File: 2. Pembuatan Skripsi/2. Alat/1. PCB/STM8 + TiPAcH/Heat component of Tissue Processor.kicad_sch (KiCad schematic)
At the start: 57 parts, among them J1 Conn_01x02, J2 Sensors, J3 Screw_Terminal_01x02, J8 Conn_01x06, K1 EE2-4.5NU, Q1 S9013, Q2 S9013, Q3 S9013, Q4 MMBT2222, SW1 SW_SPST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

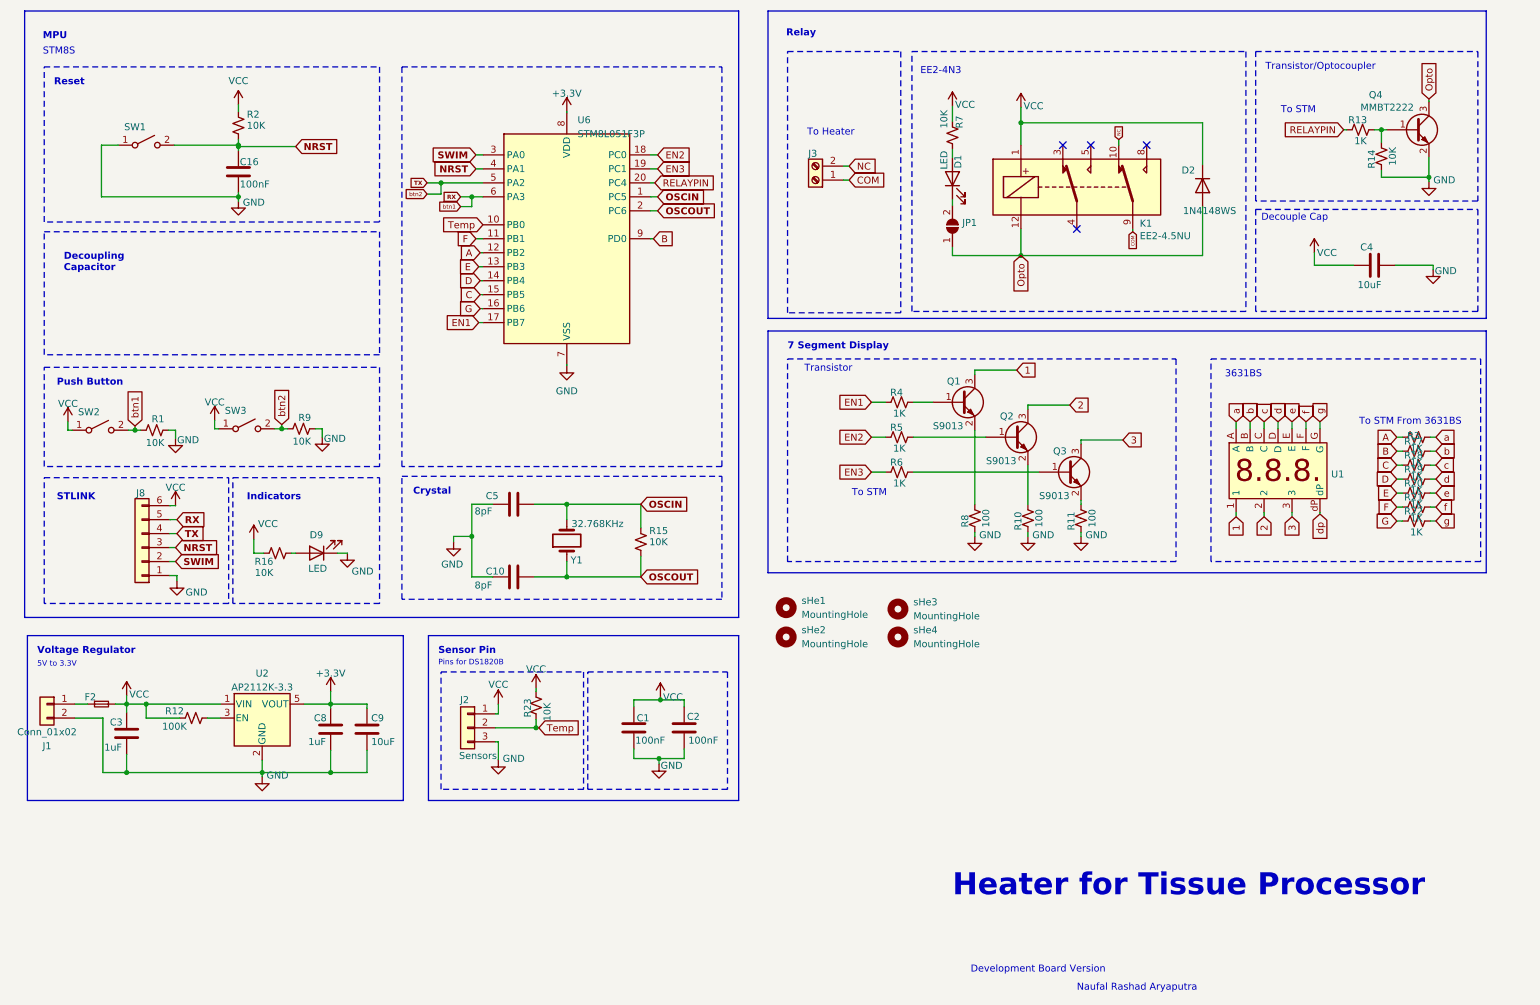
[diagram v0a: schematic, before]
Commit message: *Major Update*
- STM8S PCB jumpers are relocated to make it easier to solder it
- ATMEGA328 version is added and revised for backup option
- Arduino Code for ATMEGA328 is added.
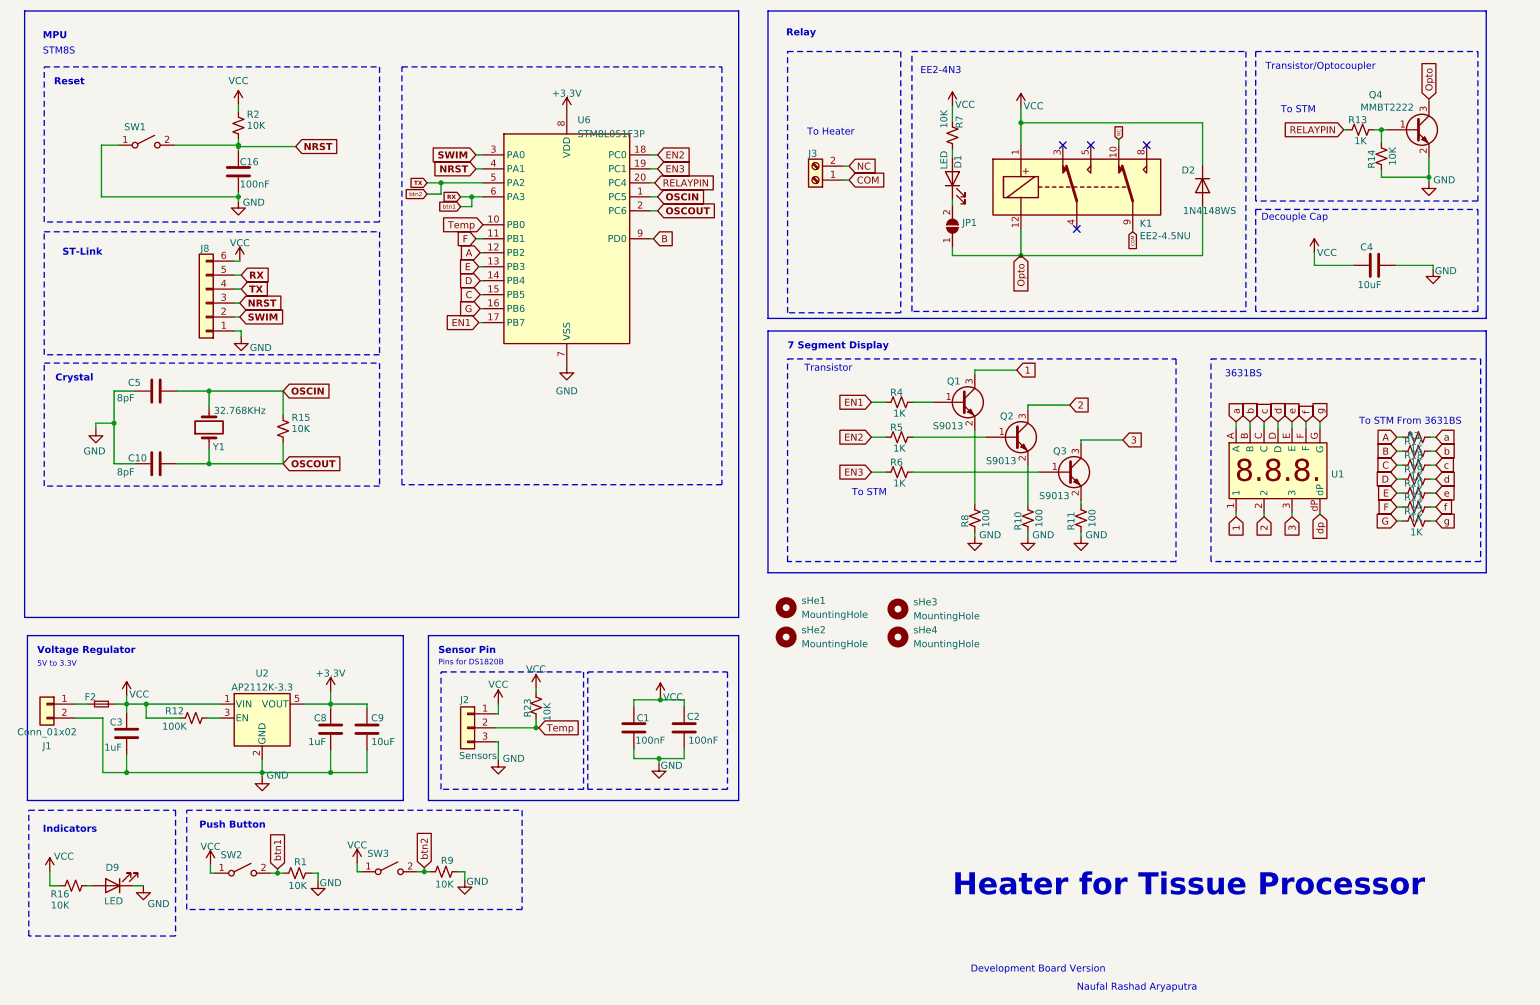
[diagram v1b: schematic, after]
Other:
- note added: "ST-Link"
- note removed: "Decoupling Capacitor"
- note removed: "STLINK"
- moved on the sheet: C10, C5, D9, J8, R1, R15, R16, R9, SW2, SW3, Y1
